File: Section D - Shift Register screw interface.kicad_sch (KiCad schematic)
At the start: 1 part

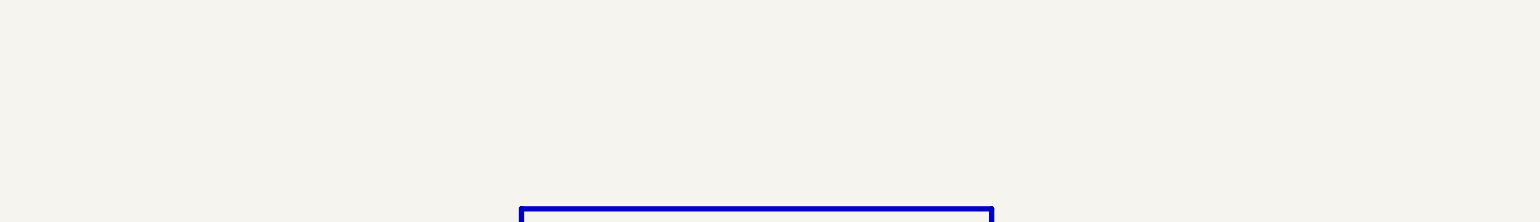
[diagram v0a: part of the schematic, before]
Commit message: minor updates of shematic and pcb and touch pad library
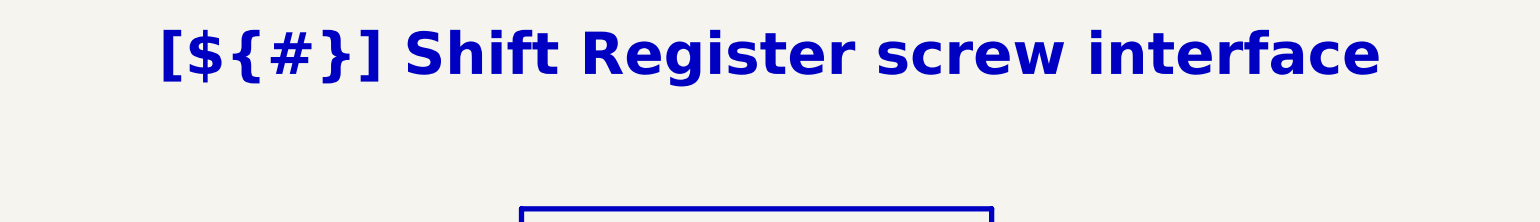
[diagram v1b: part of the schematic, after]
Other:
- title: (none) -> Shift Register screw interface
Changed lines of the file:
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@@
 	(generator_version "9.0")
 	(paper "A4")
+	(title_block
+		(title "Shift Register screw interface")
+		(date "2026-04-16")
+	)
 	(rectangle
 		(start 101.6 50.8)
@@
 		)
 	)
+	(text_box "[${#}] ${TITLE}"
+		(exclude_from_sim no)
+		(at 15.24 15.24 0)
+		(size 266.7 12.7)
+		(margins 5.9999 5.9999 5.9999 5.9999)
+		(stroke
+			(width -0.0001)
+			(type solid)
+		)
+		(fill
+			(type none)
+		)
+		(effects
+			(font
+				(face "Times New Roman")
+				(size 8 8)
+				(thickness 1.2)
+				(bold yes)
+				(color 162 22 34 1)
+			)
+		)
+	)

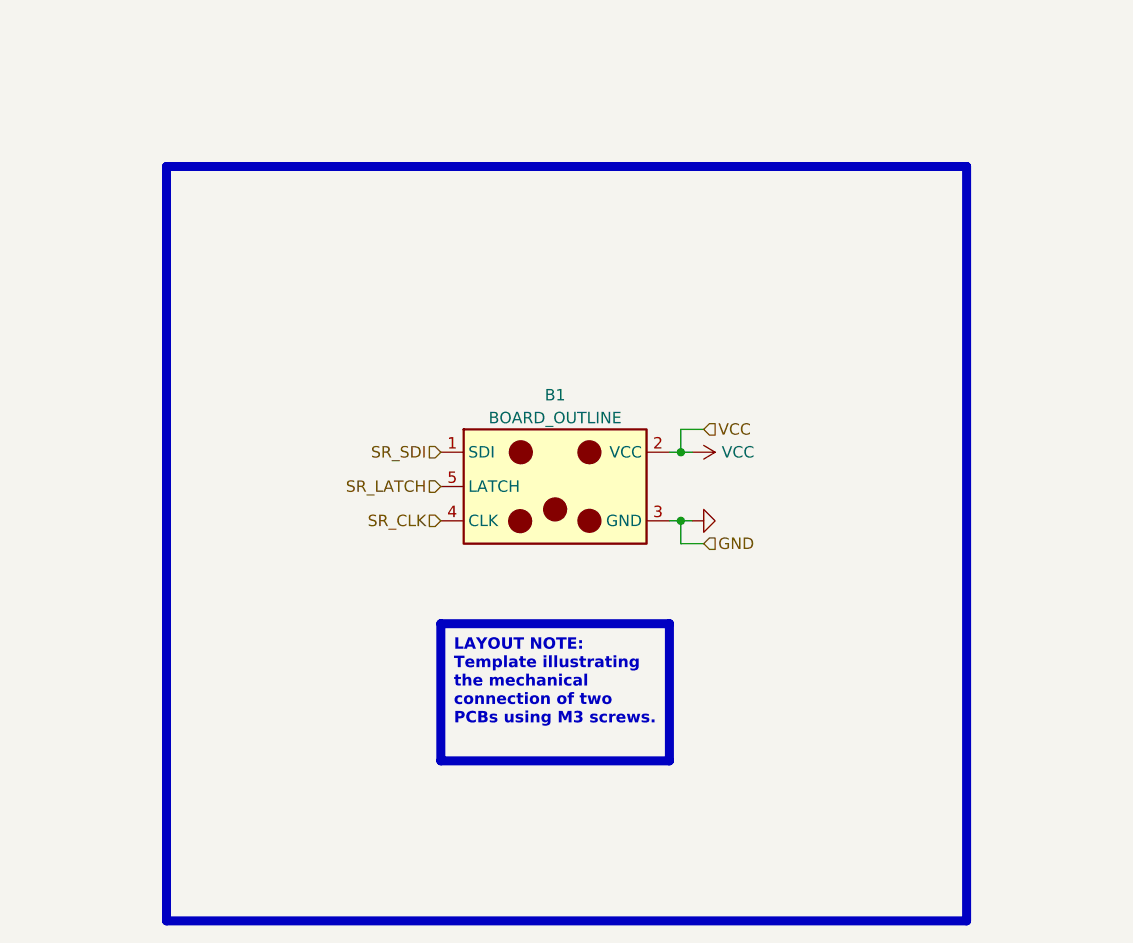
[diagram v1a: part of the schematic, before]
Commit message: screw interface update - changed pinout
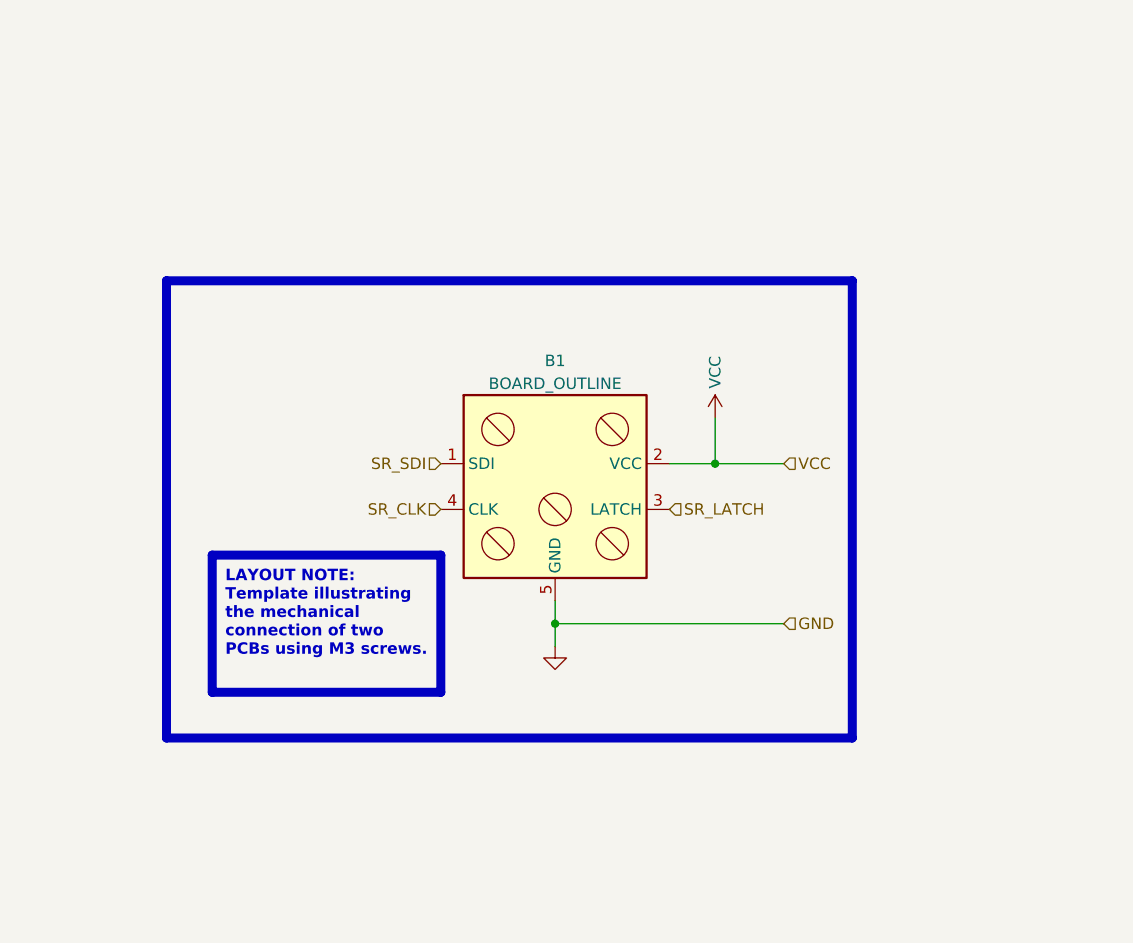
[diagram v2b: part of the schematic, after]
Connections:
- net GND: now also B1.5 (GND); no longer B1.3 (GND)
- net SR_LATCH: now also B1.3 (LATCH); no longer B1.5 (LATCH)
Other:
- moved on the sheet: B1
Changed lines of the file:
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@@
 	)
 	(rectangle
-		(start 101.6 50.8)
-		(end 190.5 134.62)
+		(start 101.6 63.5)
+		(end 177.8 114.3)
 		(stroke
 			(width 1)
@@
 	(text_box "LAYOUT NOTE:\nTemplate illustrating the mechanical connection of two PCBs using M3 screws."
 		(exclude_from_sim no)
-		(at 132.08 101.6 0)
+		(at 106.68 93.98 0)
 		(size 25.4 15.24)
 		(margins 1.4525 1.4525 1.4525 1.4525)
@@
 	)
 	(junction
-		(at 158.75 82.55)
+		(at 162.56 83.82)
 		(diameter 0)
 		(color 0 0 0 0)
 	)
 	(junction
-		(at 158.75 90.17)
+		(at 144.78 101.6)
 		(diameter 0)
 		(color 0 0 0 0)
@@
 	(wire
 		(pts
-			(xy 158.75 90.17) (xy 157.48 90.17)
-		)
-		(stroke
-			(width 0)
-			(type default)
-		)
-	)
-	(wire
-		(pts
-			(xy 158.75 80.01) (xy 158.75 82.55)
-		)
-		(stroke
-			(width 0)
-			(type default)
-		)
-	)
-	(wire
-		(pts
-			(xy 158.75 92.71) (xy 161.29 92.71)
-		)
-		(stroke
-			(width 0)
-			(type default)
-		)
-	)
-	(wire
-		(pts
-			(xy 158.75 80.01) (xy 161.29 80.01)
-		)
-		(stroke
-			(width 0)
-			(type default)
-		)
-	)
-	(wire
-		(pts
-			(xy 158.75 82.55) (xy 157.48 82.55)
-		)
-		(stroke
-			(width 0)
-			(type default)
-		)
-	)
-	(wire
-		(pts
-			(xy 158.75 90.17) (xy 158.75 92.71)
-		)
-		(stroke
-			(width 0)
-			(type default)
-		)
-	)
-	(wire
-		(pts
-			(xy 160.02 82.55) (xy 158.75 82.55)
-		)
-		(stroke
-			(width 0)
-			(type default)
-		)
-	)
-	(wire
-		(pts
-			(xy 160.02 90.17) (xy 158.75 90.17)
+			(xy 144.78 101.6) (xy 170.18 101.6)
+		)
+		(stroke
+			(width 0)
+			(type default)
+		)
+	)
+	(wire
+		(pts
+			(xy 162.56 83.82) (xy 170.18 83.82)
+		)
+		(stroke
+			(width 0)
+			(type default)
+		)
+	)
+	(wire
+		(pts
+			(xy 162.56 78.74) (xy 162.56 83.82)
+		)
+		(stroke
+			(width 0)
+			(type default)
+		)
+	)
+	(wire
+		(pts
+			(xy 144.78 101.6) (xy 144.78 104.14)
+		)
+		(stroke
+			(width 0)
+			(type default)
+		)
+	)
+	(wire
+		(pts
+			(xy 144.78 99.06) (xy 144.78 101.6)
+		)
+		(stroke
+			(width 0)
+			(type default)
+		)
+	)
+	(wire
+		(pts
+			(xy 157.48 83.82) (xy 162.56 83.82)
 		)
 		(stroke
@@
 	(hierarchical_label "VCC"
 		(shape input)
-		(at 161.29 80.01 0)
+		(at 170.18 83.82 0)
 		(effects
 			(font
@@
 	(hierarchical_label "SR_LATCH"
 		(shape input)
-		(at 132.08 86.36 180)
+		(at 157.48 88.9 0)
+		(effects
+			(font
+				(size 1.27 1.27)
+			)
+			(justify left)
+		)
+	)
+	(hierarchical_label "SR_SDI"
+		(shape input)
+		(at 132.08 83.82 180)
 		(effects
 			(font
@@
 		)
 	)
-	(hierarchical_label "SR_SDI"
-		(shape input)
-		(at 132.08 82.55 180)
-		(effects
-			(font
-				(size 1.27 1.27)
-			)
-			(justify right)
-		)
-	)
 	(hierarchical_label "GND"
 		(shape input)
-		(at 161.29 92.71 0)
+		(at 170.18 101.6 0)
 		(effects
 			(font
@@
 	(hierarchical_label "SR_CLK"
 		(shape input)
-		(at 132.08 90.17 180)
+		(at 132.08 88.9 180)
 		(effects
 			(font
@@
 	(symbol
 		(lib_id "power:GND")
-		(at 160.02 90.17 90)
+		(at 144.78 104.14 0)
 		(unit 1)
 		(exclude_from_sim no)
@@
 		(fields_autoplaced yes)
 		(property "Reference" "#PWR022"
-			(at 166.37 90.17 0)
+			(at 144.78 110.49 0)
 			(effects
 				(font
@@
 		)
 		(property "Value" "GND"
-			(at 165.1 90.17 0)
+			(at 144.78 109.22 0)
 			(effects
 				(font
@@
 		)
 		(property "Footprint" ""
-			(at 160.02 90.17 0)
+			(at 144.78 104.14 0)
 			(effects
 				(font
@@
 		)
 		(property "Datasheet" ""
-			(at 160.02 90.17 0)
+			(at 144.78 104.14 0)
 			(effects
 				(font
@@
 		)
 		(property "Description" "Power symbol creates a global label with name \"GND\" , ground"
-			(at 160.02 90.17 0)
+			(at 144.78 104.14 0)
 			(effects
 				(font
@@
 	(symbol
 		(lib_id "power:VCC")
-		(at 160.02 82.55 270)
+		(at 162.56 78.74 0)
 		(unit 1)
 		(exclude_from_sim no)
@@
 		(dnp no)
 		(property "Reference" "#PWR021"
-			(at 156.21 82.55 0)
+			(at 162.56 82.55 0)
 			(effects
 				(font
@@
 		)
 		(property "Value" "VCC"
-			(at 165.1 82.55 90)
+			(at 162.56 73.66 90)
 			(effects
 				(font
@@
 		)
 		(property "Footprint" ""
-			(at 160.02 82.55 0)
+			(at 162.56 78.74 0)
 			(effects
 				(font
@@
 		)
 		(property "Datasheet" ""
-			(at 160.02 82.55 0)
+			(at 162.56 78.74 0)
 			(effects
 				(font
@@
 		)
 		(property "Description" "Power symbol creates a global label with name \"VCC\""
-			(at 160.02 82.55 0)
+			(at 162.56 78.74 0)
 			(effects
 				(font
@@
 		(dnp no)
 		(property "Reference" "B1"
-			(at 144.78 76.2 0)
+			(at 144.78 72.39 0)
 			(effects
 				(font
@@
 		)
 		(property "Value" "BOARD_OUTLINE"
-			(at 144.78 78.74 0)
-			(effects
-				(font
+			(at 144.78 74.93 0)
+			(effects
+				(font

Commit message: [CFG] Configuration update, added bom information fields
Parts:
- B1: BOM_INFO (none) -> N/A; BOM_STATUS (none) -> OK
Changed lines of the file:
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@@
+			)
+		)
+		(property "BOM_INFO" "N/A"
+			(at 144.78 86.36 0)
+			(effects
+				(font
+					(size 1.27 1.27)
+				)
+				(hide yes)
+			)
+		)
+		(property "BOM_STATUS" "OK"
+			(at 144.78 86.36 0)
+			(effects
+				(font
+					(size 1.27 1.27)
+				)
+				(hide yes)
+			)
+		)
+		(property "Config" ""
+			(at 144.78 86.36 0)
+			(effects
+				(font
+					(size 1.27 1.27)
+				)
+				(hide yes)
+			)
+		)
+		(property "Manufacturer" ""
+			(at 144.78 86.36 0)
+			(effects
+				(font
+					(size 1.27 1.27)
+				)
+				(hide yes)
+			)
+		)
+		(property "Manufacturer Part Number" ""
+			(at 144.78 86.36 0)
+			(effects
+				(font
+					(size 1.27 1.27)
+				)
+				(hide yes)
 			)
 		)

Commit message: bom update, qr-code added
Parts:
- B1: BOM_STATUS OK -> N/A
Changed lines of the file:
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@@
 			)
 		)
-		(property "BOM_STATUS" "OK"
+		(property "BOM_STATUS" "N/A"
 			(at 144.78 86.36 0)
 			(effects

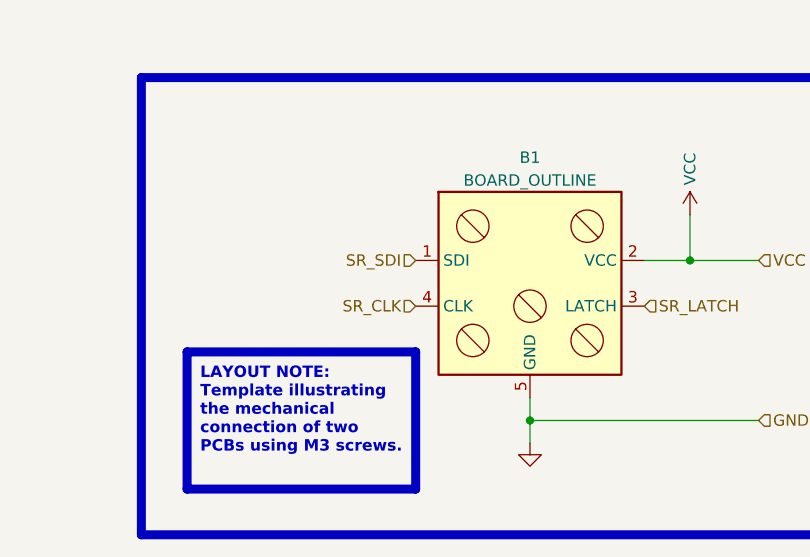
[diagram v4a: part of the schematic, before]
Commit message: [pcb] board outline/connection changed / back compatibility not possible
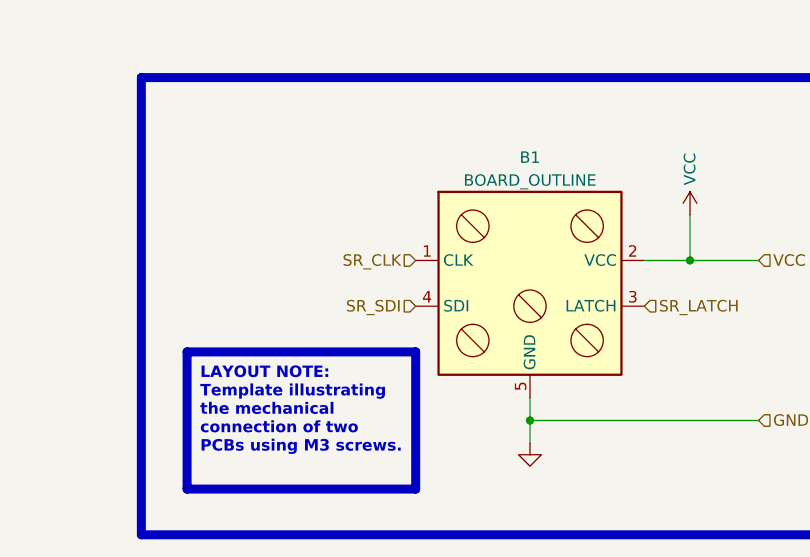
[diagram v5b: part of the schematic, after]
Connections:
- net SR_CLK: now also B1.1 (CLK); no longer B1.4 (CLK)
- net SR_SDI: now also B1.4 (SDI); no longer B1.1 (SDI)
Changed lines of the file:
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@@
 	(hierarchical_label "SR_SDI"
 		(shape input)
-		(at 132.08 83.82 180)
+		(at 132.08 88.9 180)
 		(effects
 			(font
@@
 	(hierarchical_label "SR_CLK"
 		(shape input)
-		(at 132.08 88.9 180)
+		(at 132.08 83.82 180)
 		(effects
 			(font
